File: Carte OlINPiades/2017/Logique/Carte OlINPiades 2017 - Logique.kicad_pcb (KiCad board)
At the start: 2 copper layers, 100 x 100 mm, 77 parts, among them P1 CONN_01X32, P2 CONN_01X02, P3 CONN_01X32, P4 CONN_01X05, P5 CONN_01X02, P6 CONN_01X02, U1 74AHC1G, U10 74AHC1G, U11 74AHC1G, U12 74AHC1G, U13 74AHC1G, U14 74AHC1G, U15 74AHC1G, U16 74AHC1G, U17 74AHC1G, U18 74AHC1G, U19 74AHC1G, U2 74AHC1G, U20 74AHC1G, U21 74AHC1G, U22 74AHC1G, U23 74AHC1G, U24 74AHC1G, U25 74AHC1G, U26 74AHC1G, U27 74AHC1G, U28 74AHC1G, U29 74AHC1G, U3 74AHC1G, U30 74AHC1G, U31 74AHC1G, U32 74AHC1G, U33 CD74HC154, U34 CD74HC154, U35 LM340SX, U36 74AHC1G, U37 UA78M33, U38 STM32F303K8, U4 74AHC1G, U5 74AHC1G, U6 74AHC1G, U7 74AHC1G, U8 74AHC1G, U9 74AHC1G

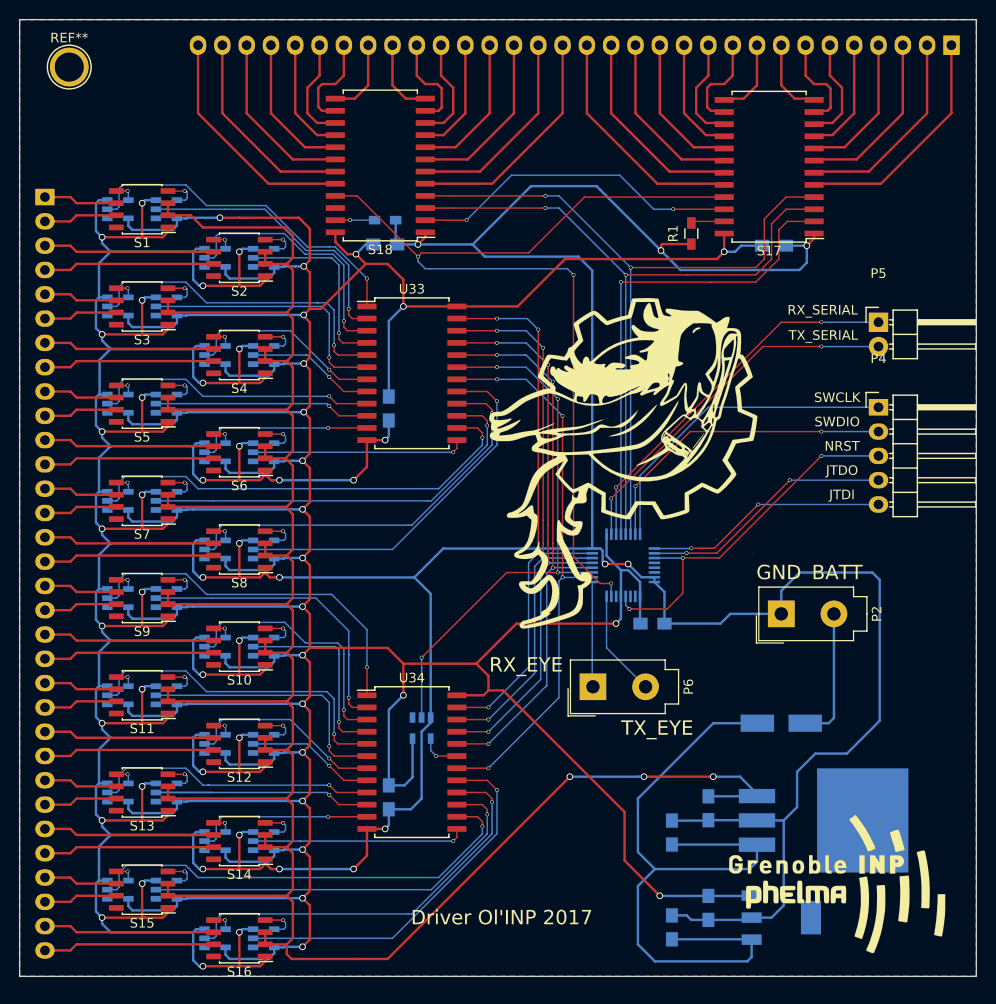
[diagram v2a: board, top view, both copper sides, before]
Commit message: Routage pour de vrai du nouveau driver Ol'INP
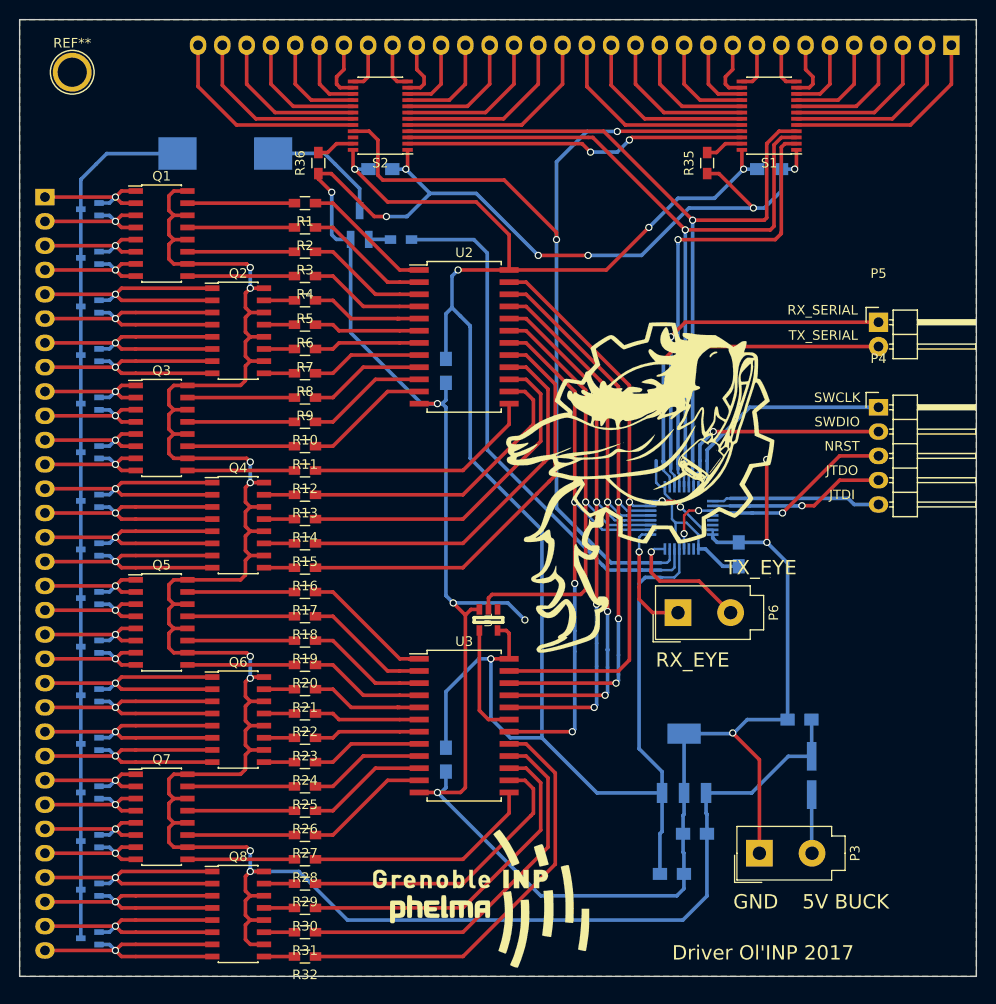
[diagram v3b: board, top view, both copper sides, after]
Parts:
- removed C9: 100nF, Capacitors_SMD:C_0805_HandSoldering
- removed S10, S11, S12, S13, S14, S15, S16, S3, S4, S5, S6, S7, S8, S9: TPS2080, Housings_SOIC:SOIC-8_3.9x4.9mm_Pitch1.27mm
- removed S17, S18: CAT4016, Housings_SOIC:SOIC-24_7.5x15.4mm_Pitch1.27mm
- removed U10, U11, U12, U13, U14, U15, U16, U17, U18, U19, U20, U21, U22, U23, U24, U25, U26, U27, U28, U29, U30, U31, U32, U36, U6, U7, U8, U9: 74AHC1G, misc:SOT-23-5
- removed U33, U34: CD74HC154, Housings_SOIC:SOIC-24_7.5x15.4mm_Pitch1.27mm
- removed U35: LM340SX, misc:TO-263-4
- removed U37: UA78M33, misc:SOT-223
- removed U38: STM32F303K8, Housings_QFP:LQFP-32_5x5mm_Pitch0.5mm
- added D10: BAT54CW, TO_SOT_Packages_SMD:SOT-323, B.Cu at (109.3, 121.5)
- added D11: BAT54CW, TO_SOT_Packages_SMD:SOT-323, B.Cu at (109.3, 126.6)
- added D12: BAT54CW, TO_SOT_Packages_SMD:SOT-323, B.Cu at (109.3, 131.7)
- added D13: BAT54CW, TO_SOT_Packages_SMD:SOT-323, B.Cu at (109.3, 136.8)
- added D14: BAT54CW, TO_SOT_Packages_SMD:SOT-323, B.Cu at (109.3, 141.9)
- added D15: BAT54CW, TO_SOT_Packages_SMD:SOT-323, B.Cu at (109.3, 146.9)
- added D16: BAT54CW, TO_SOT_Packages_SMD:SOT-323, B.Cu at (109.3, 152.0)
- added D17: RFN2L4STE25, Diodes_SMD:SMA_Handsoldering, B.Cu at (184.8, 135.0)
- added D2: BAT54CW, TO_SOT_Packages_SMD:SOT-323, B.Cu at (109.3, 80.9)
- added D3: BAT54CW, TO_SOT_Packages_SMD:SOT-323, B.Cu at (109.3, 86.0)
- added D4: BAT54CW, TO_SOT_Packages_SMD:SOT-323, B.Cu at (109.3, 91.1)
- added D5: BAT54CW, TO_SOT_Packages_SMD:SOT-323, B.Cu at (109.3, 96.1)
- added D6: BAT54CW, TO_SOT_Packages_SMD:SOT-323, B.Cu at (109.3, 101.2)
- added D7: BAT54CW, TO_SOT_Packages_SMD:SOT-323, B.Cu at (109.3, 106.3)
- added D8: BAT54CW, TO_SOT_Packages_SMD:SOT-323, B.Cu at (109.3, 111.4)
- added D9: BAT54CW, TO_SOT_Packages_SMD:SOT-323, B.Cu at (109.3, 116.5)
- added Q1: MMPQ2907A, Housings_SOIC:SOIC-16_3.9x9.9mm_Pitch1.27mm, F.Cu at (116.8, 78.4)
- added Q2: MMPQ2907A, Housings_SOIC:SOIC-16_3.9x9.9mm_Pitch1.27mm, F.Cu at (124.8, 88.5)
- added Q3: MMPQ2907A, Housings_SOIC:SOIC-16_3.9x9.9mm_Pitch1.27mm, F.Cu at (116.8, 98.7)
- added Q4: MMPQ2907A, Housings_SOIC:SOIC-16_3.9x9.9mm_Pitch1.27mm, F.Cu at (124.8, 108.8)
- added Q5: MMPQ2907A, Housings_SOIC:SOIC-16_3.9x9.9mm_Pitch1.27mm, F.Cu at (116.8, 119.0)
- added Q6: MMPQ2907A, Housings_SOIC:SOIC-16_3.9x9.9mm_Pitch1.27mm, F.Cu at (124.8, 129.2)
- added Q7: MMPQ2907A, Housings_SOIC:SOIC-16_3.9x9.9mm_Pitch1.27mm, F.Cu at (116.8, 139.3)
- added Q8: MMPQ2907A, Housings_SOIC:SOIC-16_3.9x9.9mm_Pitch1.27mm, F.Cu at (124.8, 149.5)
- added Q9: DSS4160T, TO_SOT_Packages_SMD:SOT-23_Handsoldering, B.Cu at (137.5, 77.5)
- added R10: 500, Resistors_SMD:R_0603_HandSoldering, F.Cu at (131.8, 98.0)
- added R11: 500, Resistors_SMD:R_0603_HandSoldering, F.Cu at (131.8, 100.6)
- added R12: 500, Resistors_SMD:R_0603_HandSoldering, F.Cu at (131.8, 103.1)
- added R13: 500, Resistors_SMD:R_0603_HandSoldering, F.Cu at (131.8, 105.7)
- added R14: 500, Resistors_SMD:R_0603_HandSoldering, F.Cu at (131.8, 108.2)
- added R15: 500, Resistors_SMD:R_0603_HandSoldering, F.Cu at (131.8, 110.7)
- added R16: 500, Resistors_SMD:R_0603_HandSoldering, F.Cu at (131.8, 113.3)
- added R17: 500, Resistors_SMD:R_0603_HandSoldering, F.Cu at (131.8, 115.8)
- added R18: 500, Resistors_SMD:R_0603_HandSoldering, F.Cu at (131.8, 118.4)
- added R19: 500, Resistors_SMD:R_0603_HandSoldering, F.Cu at (131.8, 120.9)
- added R20: 500, Resistors_SMD:R_0603_HandSoldering, F.Cu at (131.8, 123.4)
- added R21: 500, Resistors_SMD:R_0603_HandSoldering, F.Cu at (131.8, 126.0)
- added R22: 500, Resistors_SMD:R_0603_HandSoldering, F.Cu at (131.8, 128.5)
- added R23: 500, Resistors_SMD:R_0603_HandSoldering, F.Cu at (131.8, 131.1)
- added R24: 500, Resistors_SMD:R_0603_HandSoldering, F.Cu at (131.8, 133.6)
- added R25: 500, Resistors_SMD:R_0603_HandSoldering, F.Cu at (131.8, 136.1)
- added R26: 500, Resistors_SMD:R_0603_HandSoldering, F.Cu at (131.8, 138.7)
- added R27: 500, Resistors_SMD:R_0603_HandSoldering, F.Cu at (131.8, 141.2)
- added R28: 500, Resistors_SMD:R_0603_HandSoldering, F.Cu at (131.8, 143.8)
- added R29: 500, Resistors_SMD:R_0603_HandSoldering, F.Cu at (131.8, 146.3)
- added R3: 500, Resistors_SMD:R_0603_HandSoldering, F.Cu at (131.8, 80.3)
- added R30: 500, Resistors_SMD:R_0603_HandSoldering, F.Cu at (131.8, 148.8)
- added R31: 500, Resistors_SMD:R_0603_HandSoldering, F.Cu at (131.8, 151.4)
- added R32: 500, Resistors_SMD:R_0603_HandSoldering, F.Cu at (131.8, 153.9)
- added R33: 8.2, misc:SM_3, B.Cu at (123.5, 70.0)
- added R34: 1.7k, Resistors_SMD:R_0603_HandSoldering, B.Cu at (141.9, 79.0)
- added R35: 4k, Resistors_SMD:R_0603_HandSoldering, F.Cu at (173.9, 71.0)
- added R36: 4k, Resistors_SMD:R_0603_HandSoldering, F.Cu at (133.2, 71.0)
- added R4: 500, Resistors_SMD:R_0603_HandSoldering, F.Cu at (131.8, 82.8)
- added R5: 500, Resistors_SMD:R_0603_HandSoldering, F.Cu at (131.8, 85.3)
- added R6: 500, Resistors_SMD:R_0603_HandSoldering, F.Cu at (131.8, 87.9)
- added R7: 500, Resistors_SMD:R_0603_HandSoldering, F.Cu at (131.8, 90.4)
- added R8: 500, Resistors_SMD:R_0603_HandSoldering, F.Cu at (131.8, 93.0)
- added R9: 500, Resistors_SMD:R_0603_HandSoldering, F.Cu at (131.8, 95.5)
- C1, C2: value 100nF -> 100n
- C3: value 150nF -> 100nF
- C4: value 100nF -> 150nF
- D1: value RFN2L4STE25 -> BAT54CW; footprint Diodes_SMD:SMA_Handsoldering -> TO_SOT_Packages_SMD:SOT-323
- P2: value CONN_01X02 -> CONN_01X32; footprint Connectors_Molex_Complete:Molex_MiniFit-JR-5556-02A_2x01x4.20mm_Straight -> Pin_Headers:Pin_Header_Straight_1x32; moved to B.Cu
- P3: value CONN_01X32 -> CONN_01X02; footprint Pin_Headers:Pin_Header_Straight_1x32 -> Connectors_Molex_Complete:Molex_MiniFit-JR-5556-02A_2x01x4.20mm_Straight; moved to F.Cu
- R1: value R -> 500
- R2: value R -> 500; moved to F.Cu
- S1, S2: value TPS2080 -> CAT4016; footprint Housings_SOIC:SOIC-8_3.9x4.9mm_Pitch1.27mm -> Housings_SSOP:TSSOP-24_4.4x7.8mm_Pitch0.65mm
- U1: moved to F.Cu
- U2, U3: value 74AHC1G -> CD74HC154; footprint misc:SOT-23-5 -> Housings_SOIC:SOIC-24_7.5x15.4mm_Pitch1.27mm; moved to F.Cu
- U4: value 74AHC1G -> STM32F303K8; footprint misc:SOT-23-5 -> Housings_QFP:LQFP-32_5x5mm_Pitch0.5mm
- U5: value 74AHC1G -> UA78M33; footprint misc:SOT-23-5 -> misc:SOT-223
- moved D1 90.0 mm to (109.3, 75.8), turned to 90 degrees
- moved P3 86.8 mm to (179.3, 143.1)
- moved S1 66.3 mm to (180.3, 66.0)
- moved U5 65.9 mm to (171.4, 133.7), turned to 90 degrees
- moved P2 62.0 mm to (199.4, 58.7)
- moved C8 55.4 mm to (139.7, 71.6), turned to 0 degrees
- moved U1 54.5 mm to (151.0, 118.7), turned to 270 degrees
- moved U3 53.7 mm to (148.5, 129.8)
- moved U4 46.9 mm to (171.2, 108.1), turned to 90 degrees
- moved C2 45.0 mm to (146.6, 92.7)
- moved R1 40.5 mm to (131.8, 75.2), turned to 180 degrees
- moved G*** 37.2 mm to (150.2, 147.8)
- moved C1 37.2 mm to (146.6, 133.3)
- moved C3 29.9 mm to (177.2, 111.9), turned to 270 degrees
- moved U2 22.5 mm to (148.5, 89.2)
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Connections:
- C3 pad 1: Net-(C3-Pad1) -> GND
- C3 pad 2: GND -> +3V3
- C5 pad 1: Net-(C3-Pad1) -> +5V
- C8 pad 1: GND -> +3V3
- C8 pad 2: +3V3 -> GND
- D1 pad 1: Net-(C3-Pad1) -> Net-(D1-Pad1)
- P1 pad 1: Net-(P1-Pad1) -> Net-(D1-Pad1)
- P1 pad 2: Net-(P1-Pad2) -> Net-(D1-Pad2)
- P1 pad 3: Net-(P1-Pad3) -> Net-(D2-Pad1)
- P1 pad 4: Net-(P1-Pad4) -> Net-(D2-Pad2)
- P2 pad 1: GND -> Net-(P2-Pad1)
- P2 pad 2: Net-(D1-Pad2) -> Net-(P2-Pad2)
- P3 pad 1: Net-(P3-Pad1) -> GND
- R1 pad 1: GND -> Net-(R1-Pad1)
- R2 pad 1: GND -> Net-(R2-Pad1)
- S1 pad 2: +5V -> SERIAL_IN
- S1 pad 3: +5V -> CLK_COL
- S1 pad 4: Net-(S1-Pad4) -> LATCH_COL
- S1 pad 5: Net-(S1-Pad5) -> Net-(P2-Pad1)
- S1 pad 6: Net-(P1-Pad1) -> Net-(P2-Pad2)
- S1 pad 7: Net-(P1-Pad2) -> Net-(P2-Pad3)
- S1 pad 8: (no net) -> Net-(P2-Pad4)
- S2 pad 2: +5V -> Net-(S1-Pad22)
- S2 pad 3: +5V -> CLK_COL
- S2 pad 4: Net-(S2-Pad4) -> LATCH_COL
- S2 pad 5: Net-(S2-Pad5) -> Net-(P2-Pad17)
- S2 pad 6: Net-(P1-Pad3) -> Net-(P2-Pad18)
- S2 pad 7: Net-(P1-Pad4) -> Net-(P2-Pad19)
- S2 pad 8: (no net) -> Net-(P2-Pad20)
- U1 pad 2: Net-(U1-Pad2) -> LINE_4
- U1 pad 4: Net-(S1-Pad4) -> Net-(U1-Pad4)
- U2 pad 1: (no net) -> Net-(R1-Pad1)
- U2 pad 2: Net-(U2-Pad2) -> Net-(R2-Pad1)
- U2 pad 3: GND -> Net-(R3-Pad1)
- U2 pad 4: Net-(S2-Pad4) -> Net-(R4-Pad1)
- U2 pad 5: +3V3 -> Net-(R5-Pad1)
- U3 pad 1: (no net) -> Net-(R17-Pad1)
- U3 pad 3: GND -> Net-(R19-Pad1)
- U3 pad 5: +3V3 -> Net-(R21-Pad1)
- U4 pad 1: (no net) -> +3V3
- U4 pad 2: Net-(U33-Pad8) -> (no net)
- U4 pad 3: GND -> (no net)
- U4 pad 4: Net-(S4-Pad4) -> NRST
- U5 pad 1: (no net) -> +5V
- U5 pad 2: Net-(U33-Pad10) -> GND
- U5 pad 3: GND -> +3V3
- U5 pad 4: Net-(S5-Pad4) -> GND
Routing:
- net GND: track 717.8 -> 285.2 mm, vias 44 -> 16
- net +3V3: track 518.2 -> 226.3 mm, vias 22 -> 5
- net Net-(D1-Pad3): track 0.00 -> 90.5 mm
- net Net-(C3-Pad1): track 77.1 -> 0.00 mm
- net PURGE: track 0.00 -> 55.9 mm
- net Net-(U23-Pad2): track 47.8 -> 0.00 mm, vias 1 -> 0
- net Net-(U31-Pad2): track 47.7 -> 0.00 mm, vias 1 -> 0
- net Net-(R16-Pad1): track 0.00 -> 44.7 mm
- net Net-(R32-Pad1): track 0.00 -> 44.7 mm
- net Net-(U32-Pad2): track 43.2 -> 0.00 mm, vias 1 -> 0
- net Net-(U24-Pad2): track 43.2 -> 0.00 mm, vias 1 -> 0
- net Net-(U33-Pad15): track 43.0 -> 0.00 mm, vias 1 -> 0
- net Net-(U15-Pad2): track 43.0 -> 0.00 mm, vias 1 -> 0
- net Net-(R15-Pad1): track 0.00 -> 40.2 mm
- net Net-(R31-Pad1): track 0.00 -> 40.2 mm
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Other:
- net class Default: clearance 0.4 -> 0.1524; trace_width 0.308 -> 0.381; via_dia 0.8 -> 0.762; via_drill 0.6 -> 0.508
- net class Power_SeedStudio removed
- net class SeedStudio: trace_width 0.1524 -> 0.381; via_dia 0.4 -> 0.762; via_drill 0.3 -> 0.508
- rule trace_clearance: 0.4 -> 0.1524
- board text added: "5V BUCK"
- board text removed: "BATT"

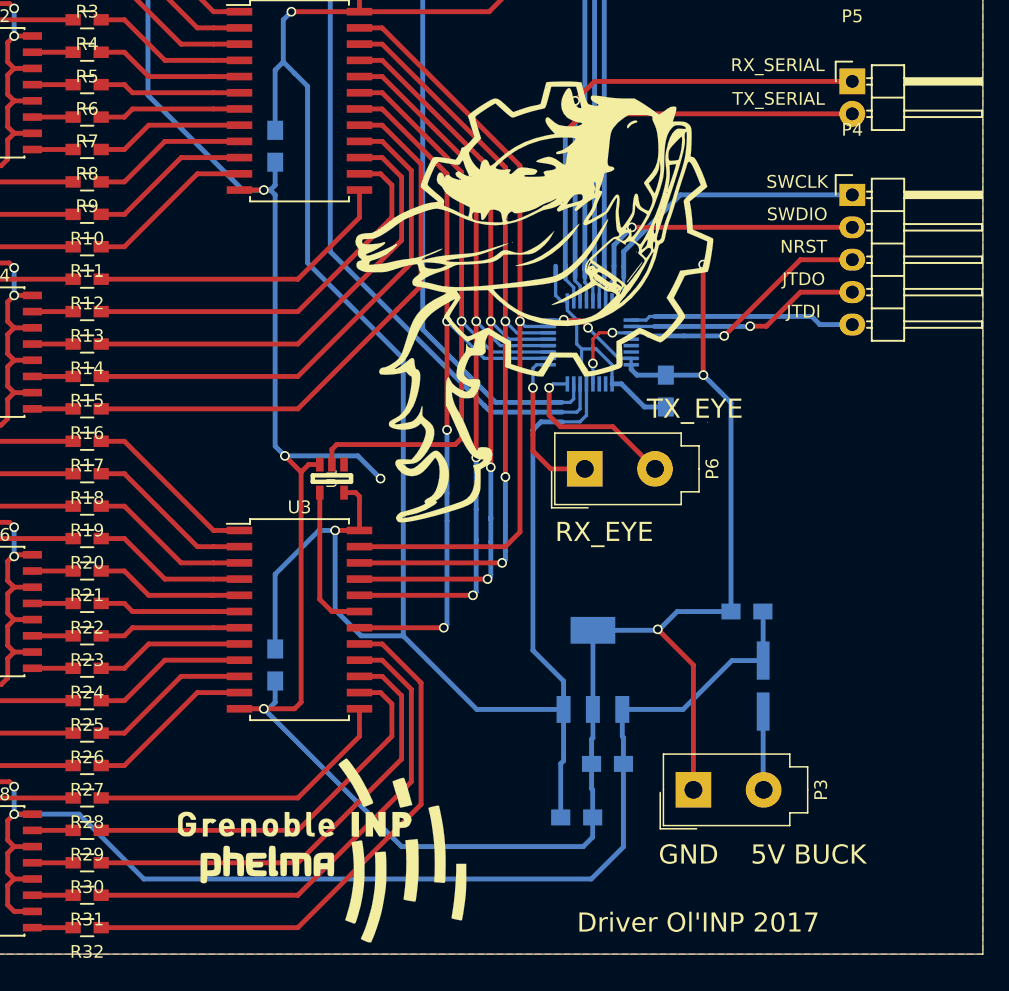
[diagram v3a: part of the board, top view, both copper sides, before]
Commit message: Passage de toute la carte en 3.3V
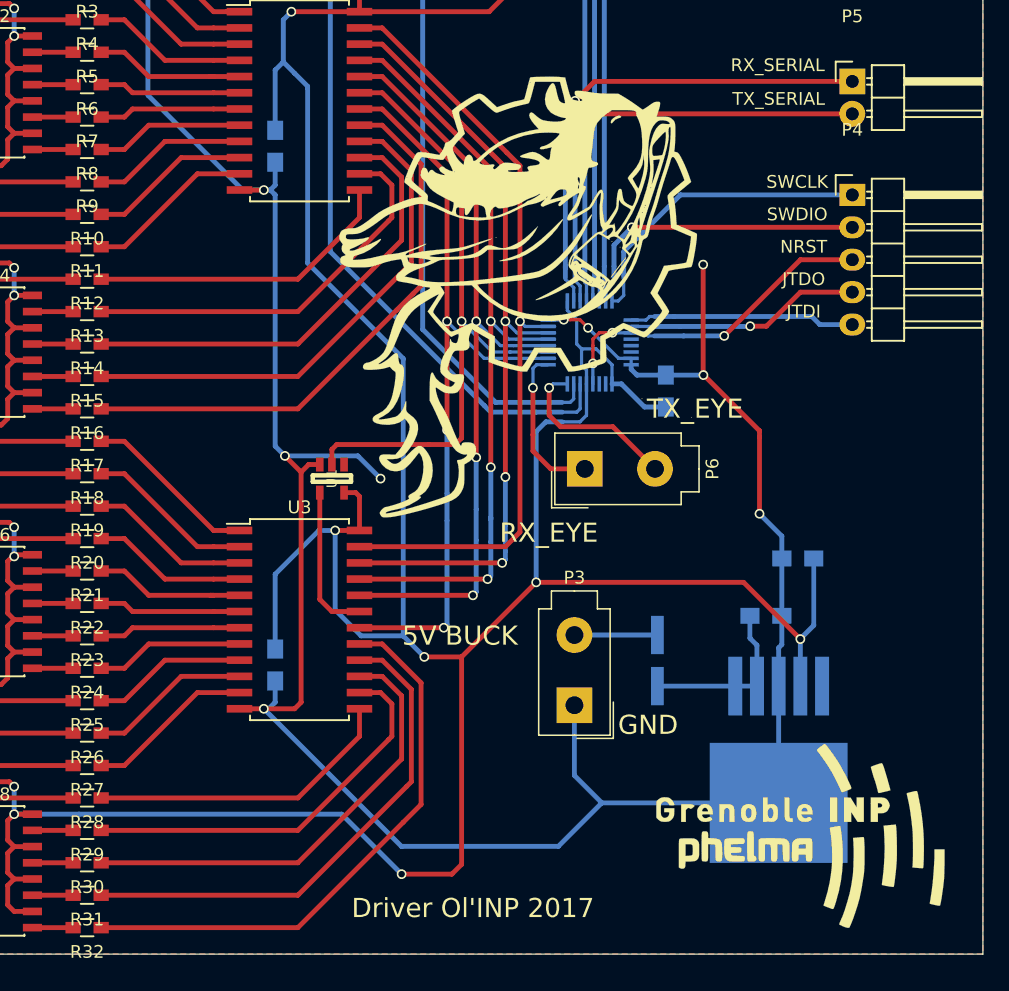
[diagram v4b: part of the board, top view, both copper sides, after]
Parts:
- removed C6: 100nF, Capacitors_SMD:C_0805_HandSoldering
- C4: value 150nF -> 1µF
- C5: value 150nF -> 47µF
- R1, R10, R11, R12, R13, R14, R15, R16, R17, R18, R19, R2, R20, R21, R22, R23, R24, R25, R26, R27, R28, R29, R3, R30, R31, R32, R4, R5, R6, R7, R8, R9: value 500 -> 470
- U5: value UA78M33 -> NCP59301DSS33R4G; footprint misc:SOT-223 -> TO_SOT_Packages_SMD:TO-263-5Lead
- moved G*** 37.5 mm to (187.7, 146.7)
- moved C5 21.9 mm to (187.5, 125.0)
- moved U5 14.6 mm to (186.0, 135.0), turned to 270 degrees
- moved P3 11.4 mm to (170.0, 136.5), turned to 180 degrees
- moved D17 8.52 mm to (176.5, 133.0), turned to 90 degrees
- moved C4 1.52 mm to (185.0, 129.5), turned to 0 degrees
- moved G*** 1.33 mm to (167.0, 104.6)
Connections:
- C5 pad 1: +5V -> +3V3
- Q1 pad 10: +5V -> +3V3
- Q1 pad 12: +5V -> +3V3
- Q1 pad 14: +5V -> +3V3
- Q1 pad 16: +5V -> +3V3
- Q2 pad 10: +5V -> +3V3
- Q2 pad 12: +5V -> +3V3
- Q2 pad 14: +5V -> +3V3
- Q2 pad 16: +5V -> +3V3
- Q3 pad 10: +5V -> +3V3
- Q3 pad 12: +5V -> +3V3
- Q3 pad 14: +5V -> +3V3
- Q3 pad 16: +5V -> +3V3
- Q4 pad 10: +5V -> +3V3
- Q4 pad 12: +5V -> +3V3
- Q4 pad 14: +5V -> +3V3
- Q4 pad 16: +5V -> +3V3
- Q5 pad 10: +5V -> +3V3
- Q5 pad 12: +5V -> +3V3
- Q5 pad 14: +5V -> +3V3
- Q5 pad 16: +5V -> +3V3
- Q6 pad 10: +5V -> +3V3
- Q6 pad 12: +5V -> +3V3
- Q6 pad 14: +5V -> +3V3
- Q6 pad 16: +5V -> +3V3
- Q7 pad 10: +5V -> +3V3
- Q7 pad 12: +5V -> +3V3
- Q7 pad 14: +5V -> +3V3
- Q7 pad 16: +5V -> +3V3
- Q8 pad 10: +5V -> +3V3
- Q8 pad 12: +5V -> +3V3
- Q8 pad 14: +5V -> +3V3
- Q8 pad 16: +5V -> +3V3
- U5 pad 2: GND -> +5V
- U5 pad 3: +3V3 -> GND
- U5 pad 4: GND -> +3V3
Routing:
- net +5V: track 256.3 -> 13.5 mm, vias 8 -> 0
- net +3V3: track 226.3 -> 466.4 mm, vias 5 -> 17
- net GND: track 285.2 -> 284.7 mm
